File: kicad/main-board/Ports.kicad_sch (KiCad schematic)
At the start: 33 parts, among them J10 690-019-298-412, J12 USB3_A, J2 HDMI_A, J3 Conn_01x10, J4 Bus_M.2_Socket_M, J5 Conn_01x10, U1 CM5108064B, U12 RT9742SNGV, U6 AP22653W6, U7 ASEK-32.768KHZ-L-R-T, U8 AP3441SHE-7B

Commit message: worked on main board
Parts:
- renumbered C13 to C?, C12 to C?, C16 to C?, C6 to C?, C19 to C?, C7 to C?, C4 to C?, C10 to C?, C14 to C?, C3 to C?, C11 to C?, C8 to C?, C15 to C?, C17 to C?, C2 to C?, D3 to D?, J10 to J?, J2 to J?, J5 to J?, J3 to J?, J12 to J?, J4 to J?, L1 to L?, R17 to R?, R15 to R?, R14 to R?, R16 to R?, R12 to R?, U12 to U?, U1 to U?, U7 to U?, U8 to U?, U6 to U?

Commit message: worke don the usb hub
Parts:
- added J14: Conn_02x01, symbol Connector_Generic:Conn_02x01
- added U14: C2684433, ProLib_pcs_2026-04-05:SSOP-16_L4.6-W2.6-P0.53-LS4.0-BL, symbol usb_hub_symbol:SL2.1S
- gave numbers to parts that had none: 33
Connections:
- net GND: now also J14.1 (Pin_1)
- net at U9.101 (USB_OTG_ID): now also J14.2 (Pin_2)
- net UDM: now reaches U9.103 (USB_N)
- net UDM: now also U9.105 (USB_P), U14.5 (UDM), U14.6 (UDP)

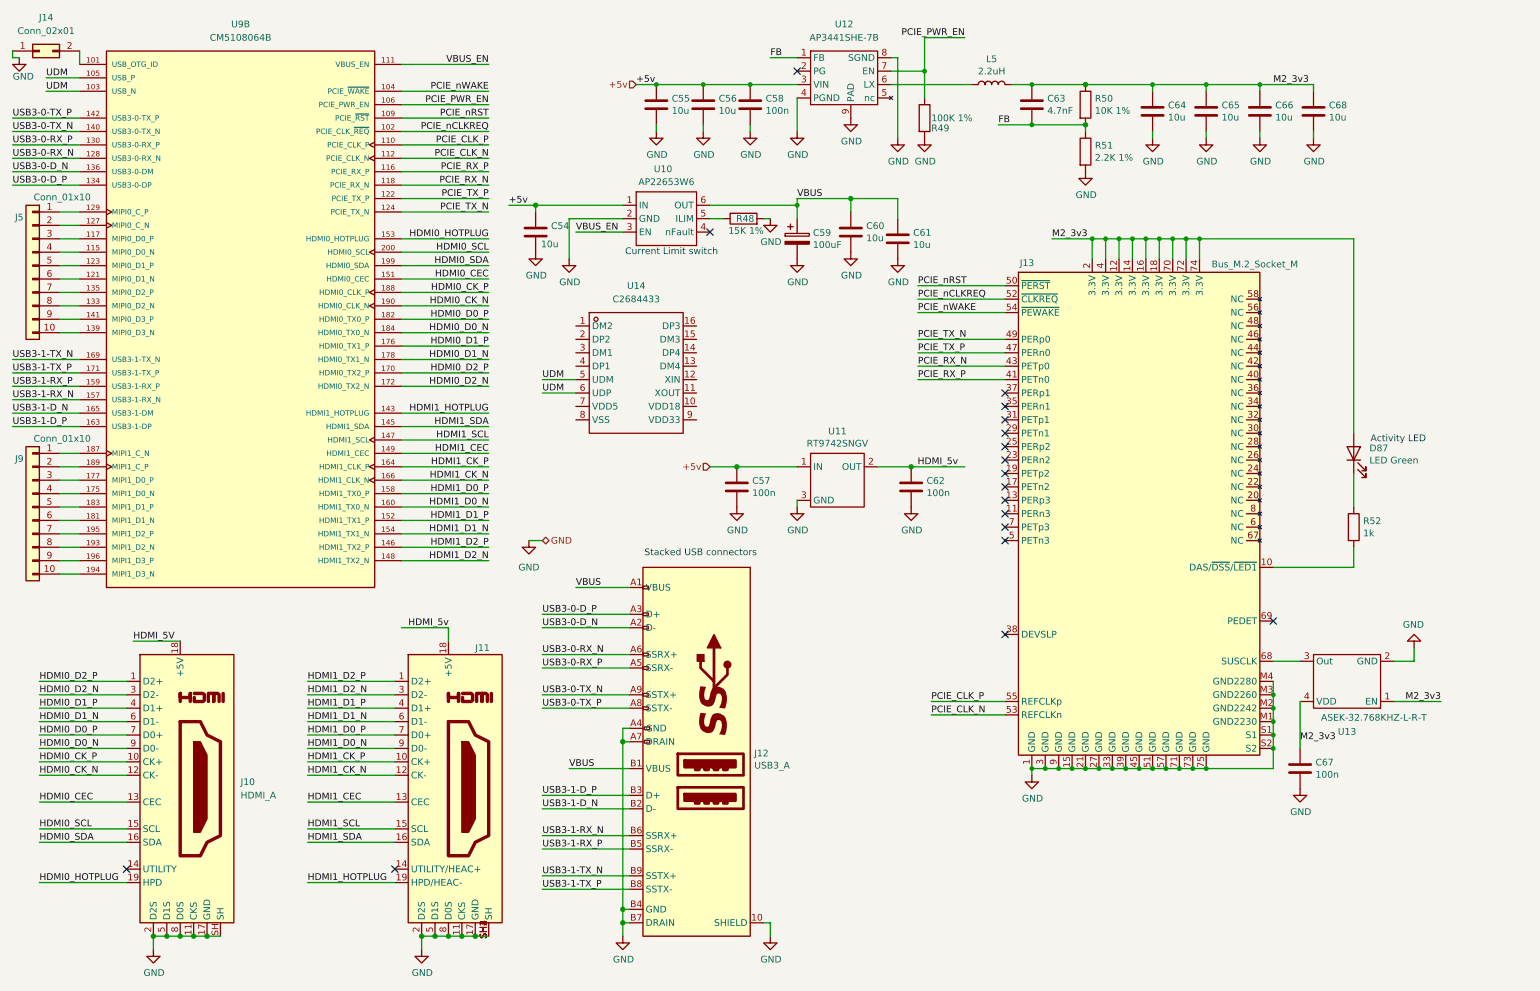
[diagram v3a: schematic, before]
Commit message: updated the main board, changes journaled in the fallout journaling
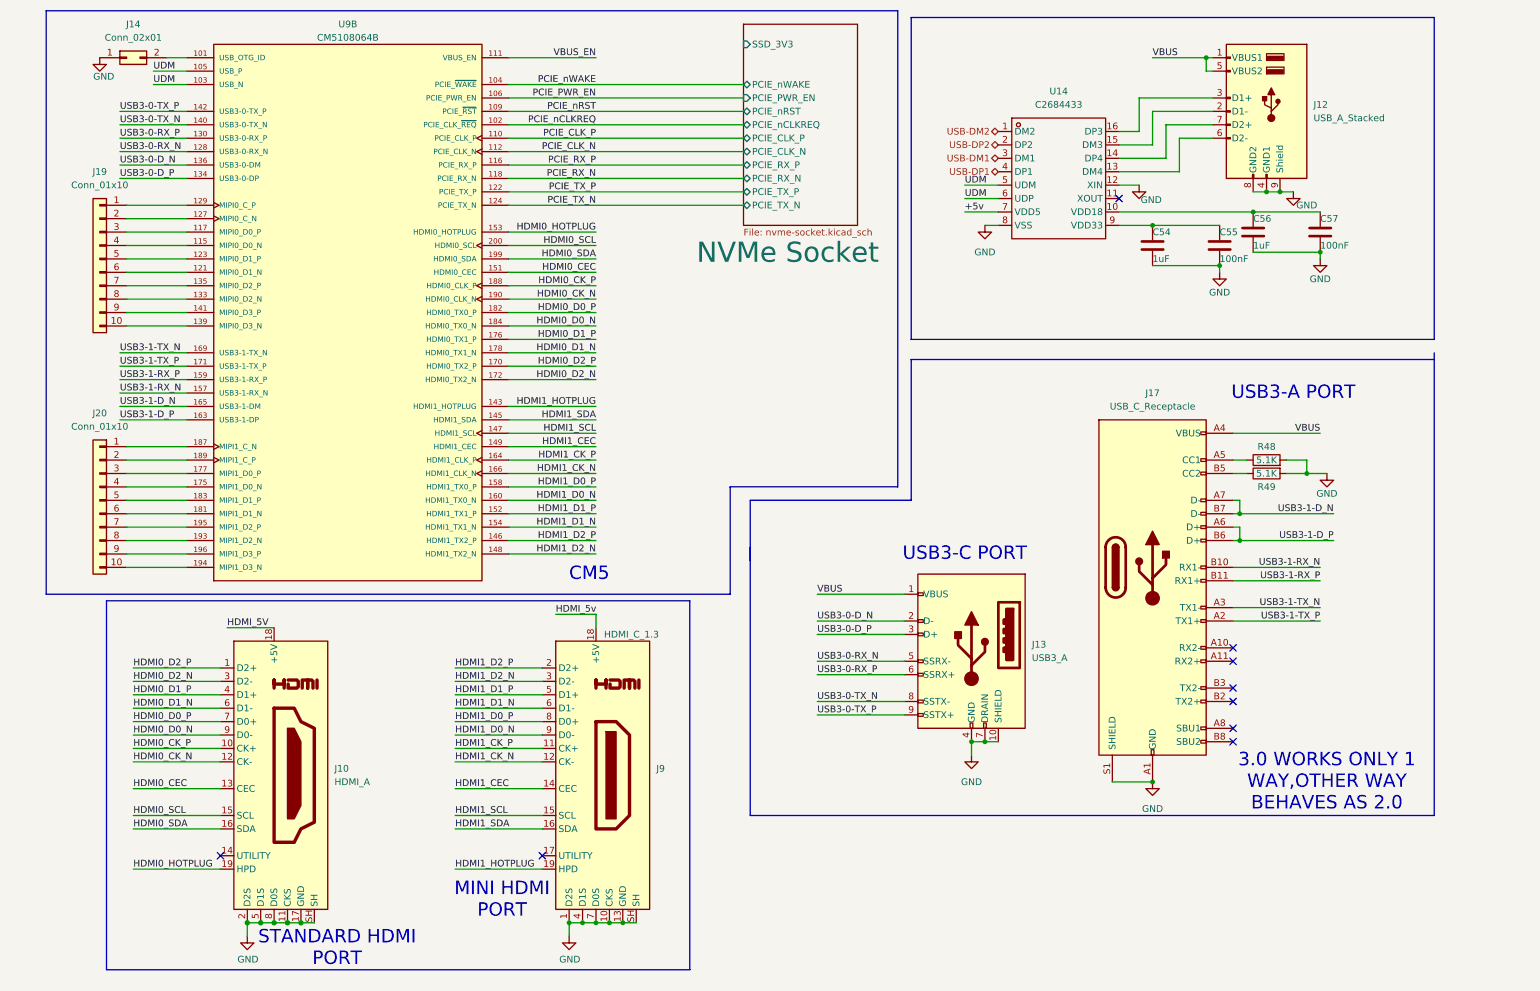
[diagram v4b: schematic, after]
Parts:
- removed C58, C62, C67: 100n, Capacitor_SMD:C_0402_1005Metric, symbol Device:C
- removed C59: 100uF, Capacitor_Tantalum_SMD:CP_EIA-7343-31_Kemet-D, symbol Device:C_Polarized
- removed C60, C61, C64, C65, C66, C68: 10u, Capacitor_SMD:C_0805_2012Metric, symbol Device:C
- removed C63: 4.7nF, Capacitor_SMD:C_0402_1005Metric, symbol Device:C
- removed D87: LED Green, LED_SMD:LED_0603_1608Metric, symbol Device:LED
- removed J11: 690-019-298-412, CM5IO:EDAC 690-019-298-412, symbol CM5IO:HDMI_A_1.4
- removed J12: USB3_A, CM5IO:MTCONN_UBAF30-D2011, symbol CM5IO:USB3_A
- removed J13: Bus_M.2_Socket_M, CM5IO:M.2 M Key socket, symbol CM5IO:Bus_M.2_Socket_M
- removed J5, J9: Conn_01x10, symbol Connector_Generic:Conn_01x10
- removed L5: 2.2uH, CM5IO:L_Bourns_SRP5030CC, symbol Device:L
- removed R50: 10K 1%, Resistor_SMD:R_0402_1005Metric, symbol Device:R
- removed R51: 2.2K 1%, Resistor_SMD:R_0402_1005Metric, symbol Device:R
- removed R52: 1k, Resistor_SMD:R_0402_1005Metric, symbol Device:R
- removed U10: AP22653W6, Package_TO_SOT_SMD:SOT-23-6, symbol CM5IO:AP2553W6
- removed U11: RT9742SNGV, Package_TO_SOT_SMD:TSOT-23_HandSoldering, symbol CM5IO:RT9742SNGV
- removed U12: AP3441SHE-7B, Package_DFN_QFN:DFN-8-1EP_2x2mm_P0.5mm_EP1.05x1.75mm, symbol CM5IO:AP3441SHE-7B
- removed U13: ASEK-32.768KHZ-L-R-T, Crystal:Crystal_SMD_3225-4Pin_3.2x2.5mm, symbol CM5IO:ASEK-32.768KHZ-L-R-T
- added J12: USB_A_Stacked, symbol Connector:USB_A_Stacked
- added J13: USB3_A, symbol Connector:USB3_A
- added J17: USB_C_Receptacle, symbol Connector:USB_C_Receptacle
- added J19, J20: Conn_01x10, symbol Connector_Generic:Conn_01x10
- added J9: HDMI_C_1.3, symbol Connector:HDMI_C_1.3
- C54, C56: value 10u -> 1uF; footprint Capacitor_SMD:C_0805_2012Metric -> (none); Field4 Digikey -> (none); Field5 490-14381-1-ND -> (none); Field6 GRM21BR71A106KA73L -> (none); Field7 Murata -> (none); Field8 111893011 -> (none); Part Description 10uF 10% 10V Ceramic Capacitor X7R 0805 (2012 Metric) -> (none)
- C55: value 10u -> 100nF; footprint Capacitor_SMD:C_0805_2012Metric -> (none); Field4 Digikey -> (none); Field5 490-14381-1-ND -> (none); Field6 GRM21BR71A106KA73L -> (none); Field7 Murata -> (none); Field8 111893011 -> (none); Part Description 10uF 10% 10V Ceramic Capacitor X7R 0805 (2012 Metric) -> (none)
- C57: value 100n -> 100nF; footprint Capacitor_SMD:C_0402_1005Metric -> (none); Field4 Farnell -> (none); Field5 2611911 -> (none); Field6 RM EMK105 B7104KV-F -> (none); Field7 TAIYO YUDEN EUROPE GMBH -> (none); Field8 110091611 -> (none); Part Description 0.1uF 10% 16V Ceramic Capacitor X7R 0402 (1005 Metric) -> (none)
- R48: value 15K 1% -> 5.1K; footprint Resistor_SMD:R_0402_1005Metric -> (none); Field4 Farnell -> (none); Field5 9239375 -> (none); Field6 MCR01MZPF1502 -> (none); Field7 Rohm -> (none); Field8 120891581 -> (none); Part Description Resistor 15K M1005 1% 63mW -> (none)
- R49: value 100K 1% -> 5.1K; footprint Resistor_SMD:R_0402_1005Metric -> (none); Field4 Farnell -> (none); Field6 MCR01MZPF1003 -> (none); Field7 Rohm -> (none); Part Description Resistor 100K M1005 1% 63mW -> (none)
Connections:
- net +5v: now also U14.7 (VDD5); no longer C54.1, C55.1, C56.1, C57.1
- net GND: now also U14.12 (XIN), U14.8 (VSS), J12.4 (GND1), J12.8 (GND2), J12.9 (Shield), J13.10 (SHIELD), J13.4 (GND), J13.7 (DRAIN), J17.A1 (GND), J17.A12 (GND), J17.B1 (GND), J17.B12 (GND), J17.S1 (SHIELD), J9.1 (D2S), J9.10 (CKS), J9.13 (GND), J9.4 (D1S), J9.7 (D0S), J9.SH
- net HDMI1_CEC: now also J9.14 (CEC)
- net HDMI1_CK_N: now also J9.12 (CK-)
- net HDMI1_CK_P: now also J9.11 (CK+)
- net HDMI1_D0_N: now also J9.9 (D0-)
- net HDMI1_D0_P: now also J9.8 (D0+)
- net HDMI1_D1_N: now also J9.6 (D1-)
- net HDMI1_D1_P: now also J9.5 (D1+)
- net HDMI1_D2_N: now also J9.3 (D2-)
- net HDMI1_D2_P: now also J9.2 (D2+)
- net HDMI1_HOTPLUG: now also J9.19 (HPD)
- net HDMI1_SCL: now also J9.15 (SCL)
- net HDMI1_SDA: now also J9.16 (SDA)
- net HDMI_5v: now also J9.18 (+5V)
- net PCIE_PWR_EN: no longer R49.1
- net USB3-0-D_N: now also J13.2 (D-)
- net USB3-0-D_P: now also J13.3 (D+)
- net USB3-0-RX_N: now also J13.5 (SSRX-)
- net USB3-0-RX_P: now also J13.6 (SSRX+)
- net USB3-0-TX_N: now also J13.8 (SSTX-)
- net USB3-0-TX_P: now also J13.9 (SSTX+)
- net USB3-1-D_N: now also J17.A7 (D-), J17.B7 (D-)
- net USB3-1-D_P: now also J17.A6 (D+), J17.B6 (D+)
- net USB3-1-RX_N: now also J17.B10 (RX1-)
- net USB3-1-RX_P: now also J17.B11 (RX1+)
- net USB3-1-TX_N: now also J17.A3 (TX1-)
- net USB3-1-TX_P: now also J17.A2 (TX1+)
- net VBUS: now also J12.1 (VBUS1), J12.5 (VBUS2), J13.1 (VBUS), J17.A4 (VBUS), J17.A9 (VBUS), J17.B4 (VBUS), J17.B9 (VBUS)
- net at U9.115 (MIPI0_D0_N): now also J19.4 (Pin_4)
- net at U9.117 (MIPI0_D0_P): now also J19.3 (Pin_3)
- net at U9.121 (MIPI0_D1_N): now also J19.6 (Pin_6)
- net at U9.123 (MIPI0_D1_P): now also J19.5 (Pin_5)
- net at U9.127 (MIPI0_C_N): now also J19.2 (Pin_2)
- net at U9.129 (MIPI0_C_P): now also J19.1 (Pin_1)
- net at U9.133 (MIPI0_D2_N): now also J19.8 (Pin_8)
- net at U9.135 (MIPI0_D2_P): now also J19.7 (Pin_7)
- net at U9.139 (MIPI0_D3_N): now also J19.10 (Pin_10)
- net at U9.141 (MIPI0_D3_P): now also J19.9 (Pin_9)
- net at U9.175 (MIPI1_D0_N): now also J20.4 (Pin_4)
- net at U9.177 (MIPI1_D0_P): now also J20.3 (Pin_3)
- net at U9.181 (MIPI1_D1_N): now also J20.6 (Pin_6)
- net at U9.183 (MIPI1_D1_P): now also J20.5 (Pin_5)
- net at U9.187 (MIPI1_C_N): now also J20.1 (Pin_1)
- net at U9.189 (MIPI1_C_P): now also J20.2 (Pin_2)
- net at U9.193 (MIPI1_D2_N): now also J20.8 (Pin_8)
- net at U9.194 (MIPI1_D3_N): now also J20.10 (Pin_10)
- net at U9.195 (MIPI1_D2_P): now also J20.7 (Pin_7)
- net at U9.196 (MIPI1_D3_P): now also J20.9 (Pin_9)
- net USB-DM2: now reaches U14.1 (DM2)
- net at U14.10 (VDD18): now also C56.1, C57.1
- net at U14.13 (DM4): now also J12.6 (D2-)
- net at U14.14 (DP4): now also J12.7 (D2+)
- net at U14.15 (DM3): now also J12.2 (D1-)
- net at U14.16 (DP3): now also J12.3 (D1+)
- net USB-DP2: now reaches U14.2 (DP2)
- net USB-DM1: now reaches U14.3 (DM1)
- net USB-DP1: now reaches U14.4 (DP1)
- net at U14.9 (VDD33): now also C54.1, C55.1
- net at R48.1: now also J17.A5 (CC1)
- new net: J17.B5 (CC2), R49.1
- no-connect marks 18 -> 9
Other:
- added sheet NVMe Socket (nvme-socket.kicad_sch)
- note added: "3.0 WORKS ONLY 1 WAY,OTHER WAY BEHAVES AS 2.0"
- note added: "CM5"
- note added: "MINI HDMI PORT"
- note added: "STANDARD HDMI PORT"
- note added: "USB3-A PORT"
- note added: "USB3-C PORT"
- note removed: "Activity LED"
- note removed: "Current Limit switch"
- note removed: "Stacked USB connectors"
- moved on the sheet: J10, J14, U14, U9B

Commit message: Completed the main board schematic
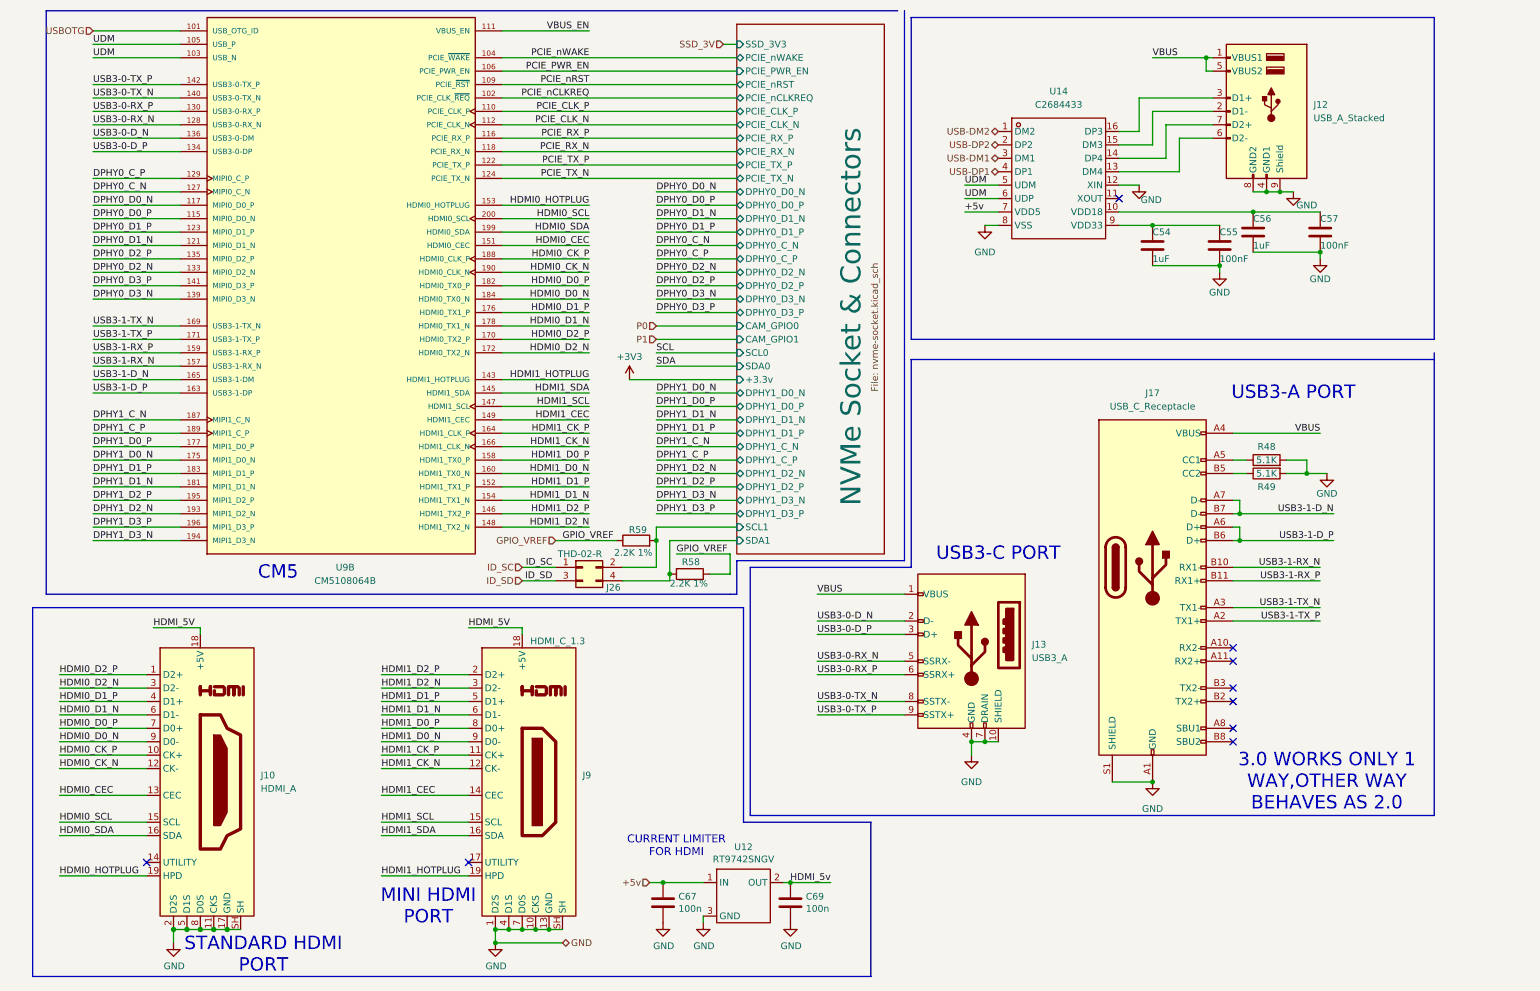
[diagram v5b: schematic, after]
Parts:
- removed J14: Conn_02x01, symbol Connector_Generic:Conn_02x01
- removed J19, J20: Conn_01x10, symbol Connector_Generic:Conn_01x10
- added C67, C69: 100n, Capacitor_SMD:C_0402_1005Metric, symbol Device:C
- added J26: THD-02-R, Connector_PinHeader_2.54mm:PinHeader_2x02_P2.54mm_Vertical, symbol Connector_Generic:Conn_02x02_Odd_Even
- added R58, R59: 2.2K 1%, Resistor_SMD:R_0402_1005Metric, symbol Device:R
- added U12: RT9742SNGV, Package_TO_SOT_SMD:TSOT-23_HandSoldering, symbol CM5IO:RT9742SNGV
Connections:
- net +5v: now also C67.1, U12.1 (IN)
- net GND: now also C67.2, C69.2, U12.3 (GND)
- net HDMI_5V: now also J9.18 (+5V)
- net HDMI_5v: now also C69.1, U12.2 (OUT); no longer J9.18 (+5V)
- net USBOTG: now reaches U9.101 (USB_OTG_ID)
- net DPHY0_D0_P: now reaches U9.115 (MIPI0_D0_N)
- net DPHY0_D0_N: now reaches U9.117 (MIPI0_D0_P)
- net DPHY0_D1_N: now reaches U9.121 (MIPI0_D1_N)
- net DPHY0_D1_P: now reaches U9.123 (MIPI0_D1_P)
- net DPHY0_C_N: now reaches U9.127 (MIPI0_C_N)
- net DPHY0_C_P: now reaches U9.129 (MIPI0_C_P)
- net DPHY0_D2_N: now reaches U9.133 (MIPI0_D2_N)
- net DPHY0_D2_P: now reaches U9.135 (MIPI0_D2_P)
- net DPHY0_D3_N: now reaches U9.139 (MIPI0_D3_N)
- net DPHY0_D3_P: now reaches U9.141 (MIPI0_D3_P)
- net DPHY1_D0_N: now reaches U9.175 (MIPI1_D0_N)
- net DPHY1_D0_P: now reaches U9.177 (MIPI1_D0_P)
- net DPHY1_D1_N: now reaches U9.181 (MIPI1_D1_N)
- net DPHY1_D1_P: now reaches U9.183 (MIPI1_D1_P)
- net DPHY1_C_N: now reaches U9.187 (MIPI1_C_N)
- net DPHY1_C_P: now reaches U9.189 (MIPI1_C_P)
- net DPHY1_D2_N: now reaches U9.193 (MIPI1_D2_N)
- net DPHY1_D3_N: now reaches U9.194 (MIPI1_D3_N)
- net DPHY1_D2_P: now reaches U9.195 (MIPI1_D2_P)
- net DPHY1_D3_P: now reaches U9.196 (MIPI1_D3_P)
- new net GPIO_VREF: R58.1, R59.1
- new net ID_SC: J26.1 (Pin_1)
- new net ID_SD: J26.3 (Pin_3)
- new net NVMe Socket & Connectors/SCL1: J26.2 (Pin_2), R59.2
- new net NVMe Socket & Connectors/SDA1: J26.4 (Pin_4), R58.2
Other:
- sheet NVMe Socket renamed NVMe Socket & Connectors
- sheet NVMe Socket & Connectors ports: added +3.3v, CAM_GPIO0, CAM_GPIO1, DPHY0_C_N, DPHY0_C_P, DPHY0_D0_N, DPHY0_D0_P, DPHY0_D1_N, DPHY0_D1_P, DPHY0_D2_N, DPHY0_D2_P, DPHY0_D3_N, DPHY0_D3_P, DPHY1_C_N, DPHY1_C_P, DPHY1_D0_N, DPHY1_D0_P, DPHY1_D1_N, DPHY1_D1_P, DPHY1_D2_N, DPHY1_D2_P, DPHY1_D3_N, DPHY1_D3_P, SCL0, SCL1, SDA0, SDA1; removed none
- note added: "CURRENT LIMITER FOR HDMI"
- moved on the sheet: J10, J9, U9B

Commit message: finally completed the schematic
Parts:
- removed J12: USB_A_Stacked, symbol Connector:USB_A_Stacked
- added C85, C87: 1uF, symbol Device:C
- added C86, C88: 100nF, symbol Device:C
- added J43: USB_A_Stacked, symbol Connector:USB_A_Stacked
- added J44: USB_A, symbol Connector:USB_A
- added U23: C2684433, ProLib_pcs_2026-04-05:SSOP-16_L4.6-W2.6-P0.53-LS4.0-BL, symbol usb_hub_symbol:SL2.1S
- renumbered C56 to C89, C57 to C90, C54 to C91, C55 to C92, C67 to C93, C69 to C94, J17 to J48, J26 to J49, J13 to J50, J10 to J51, J9 to J52, R48 to R65, R49 to R66, R59 to R67, R58 to R68, U14 to U24, U12 to U25, U9 to U3
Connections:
- net +5v: now also U23.7 (VDD5)
- net GND: now also C85.2, C86.2, C87.2, C88.2, J43.4 (GND1), J43.8 (GND2), J43.9 (Shield), J44.4 (GND), J44.5 (Shield), U23.12 (XIN), U23.8 (VSS)
- net VBUS: now also J43.1 (VBUS1), J43.5 (VBUS2), J44.1 (VBUS)
- net USB-DM4: now reaches U24.13 (DM4)
- net USB-DP4: now reaches U24.14 (DP4)
- net at U24.15 (DM3): now also U23.5 (UDM)
- net at U24.16 (DP3): now also U23.6 (UDP)
- new net: J43.2 (D1-), U23.1 (DM2)
- new net: C85.1, C86.1, U23.10 (VDD18)
- new net: J44.2 (D-), U23.13 (DM4)
- new net: J44.3 (D+), U23.14 (DP4)
- new net: J43.3 (D1+), U23.2 (DP2)
- new net: J43.6 (D2-), U23.3 (DM1)
- new net: J43.7 (D2+), U23.4 (DP1)
- new net: C87.1, C88.1, U23.9 (VDD33)
- new net USB-DM3: U23.15 (DM3)
- new net USB-DP3: U23.16 (DP3)
- no-connect marks 9 -> 10
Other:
- sheet NVMe Socket & Connectors ports: added SSD_3V; removed SSD_3V3
- note added: "CIPHER - by ARYAN-GIT-BYTE"
- moved on the sheet: C89, C90, C91, C92, J48, R65, R66, U24

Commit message: DOCUMENTED Till the Navigation board
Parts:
- renumbered C85 to C79, C86 to C80, C87 to C81, C88 to C82, C89 to C83, C90 to C84, C91 to C85, C92 to C86, C93 to C87, C94 to C88, J48 to J45, J49 to J46, J50 to J47, J51 to J48, J52 to J49, U24 to U22, U25 to U23, U23 to U8

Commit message: changed buck converters
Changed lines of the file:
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@@
 	(polyline
 		(pts
-			(xy 281.94 165.1) (xy 281.94 77.47)
+			(xy 281.94 165.1) (xy 281.94 78.74)
 		)
 		(stroke
@@
 	(polyline
 		(pts
-			(xy 19.05 12.7) (xy 180.34 12.7)
-		)
-		(stroke
+			(xy 19.05 12.7) (xy 181.61 12.7)
+		)
+		(stroke
